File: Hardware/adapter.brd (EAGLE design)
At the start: 61.9 x 62.5 mm, 8 parts

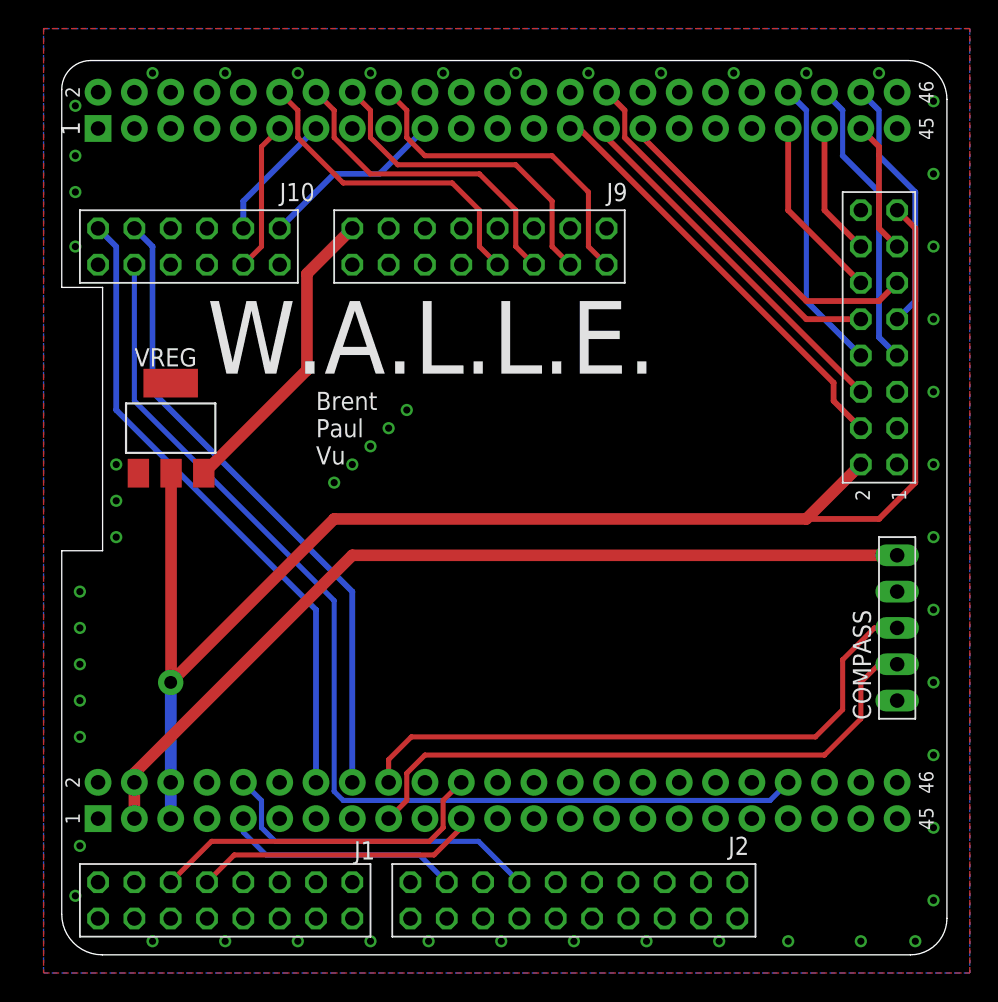
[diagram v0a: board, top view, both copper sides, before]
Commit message: Converted to TI LDO component.
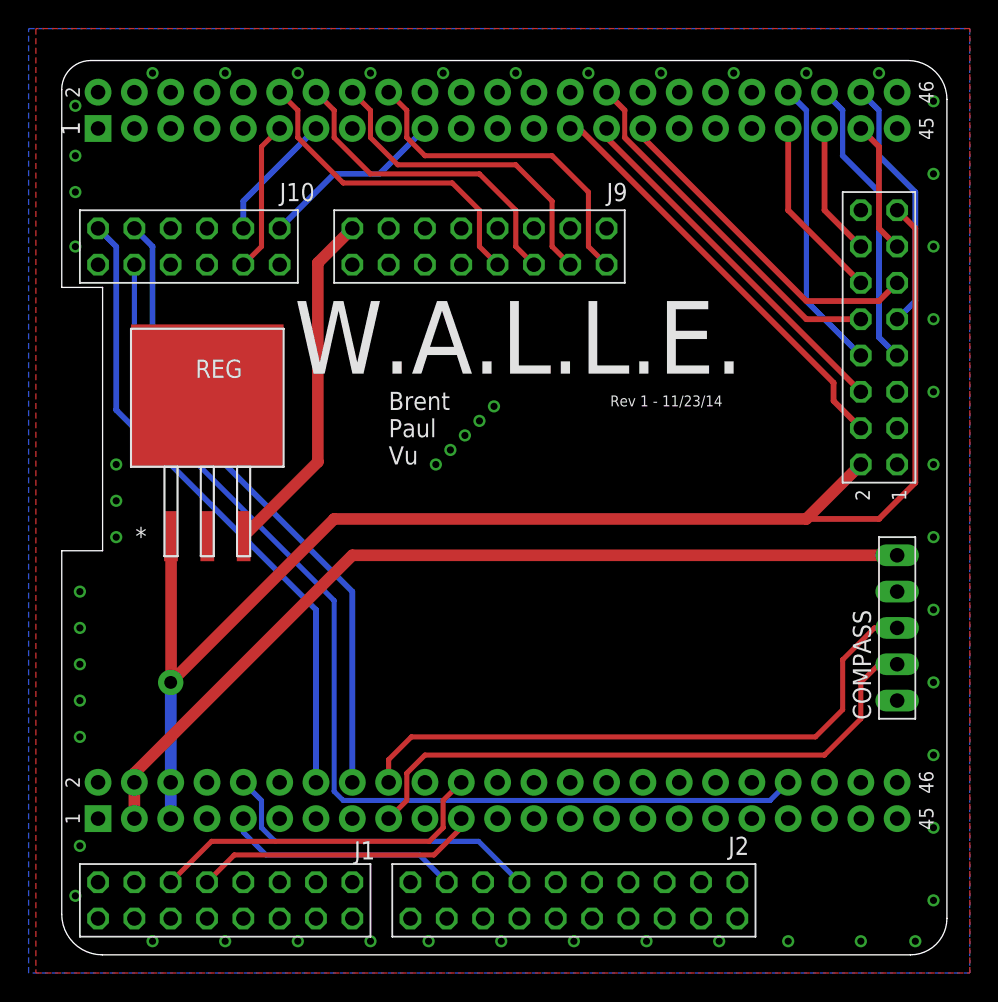
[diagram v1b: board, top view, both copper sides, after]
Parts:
- removed VREG: REG1117, burr-brown:SOT223
- added REG: UCC383-5_KTT_3, TI_UCC:KTT3_6P22X6P6
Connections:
- net 5V: now also REG.1; no longer VREG.2
- net GND: now also REG.2, REG.4; no longer VREG.1
- net VBAT: now also REG.3; no longer VREG.3
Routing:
- net 5V: track 121.6 -> 102.5 mm
- net VBAT: track 21.4 -> 24.7 mm
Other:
- board text added: "Rev 1 - 11/23/14"
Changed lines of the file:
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@@
 <setting verticaltext="up"/>
 </settings>
-<grid distance="0.4" unitdist="mil" unit="mil" style="lines" multiple="1" display="yes" altdistance="10" altunitdist="mil" altunit="mil"/>
+<grid distance="40" unitdist="mil" unit="mil" style="lines" multiple="1" display="yes" altdistance="10" altunitdist="mil" altunit="mil"/>
 <layers>
 <layer number="1" name="Top" color="4" fill="1" visible="yes" active="yes"/>
@@
 <wire x1="26.67" y1="47.9425" x2="29.5275" y2="47.9425" width="0" layer="20"/>
 <wire x1="29.5275" y1="29.5275" x2="26.67" y2="29.5275" width="0" layer="20"/>
-<text x="36.83" y="41.91" size="5.08" layer="21">W.A.L.L.E.</text>
-<text x="44.45" y="35.56" size="1.27" layer="21">Brent
+<text x="42.926" y="41.91" size="5.08" layer="21">W.A.L.L.E.</text>
+<text x="49.53" y="35.56" size="1.27" layer="21">Brent
 Paul
 Vu</text>
@@
 <text x="85.725" y="33.02" size="1.016" layer="25" rot="R90">1</text>
 <text x="83.185" y="33.02" size="1.016" layer="25" rot="R90">2</text>
+<text x="65.024" y="39.624" size="0.762" layer="21">Rev 1 - 11/23/14</text>
 </plain>
 <attributes>
@@
 <attribute name="VALUE" x="66.04" y="46.355" size="1.27" layer="28" rot="MR0"/>
 </element>
-<element name="VREG" library="burr-brown" package="SOT223" value="REG1117" x="34.29" y="38.1">
-<attribute name="OC_NEWARK" value="14P6981" x="34.29" y="38.1" size="1.778" layer="27" display="off"/>
-<attribute name="MPN" value="REG1117" x="34.29" y="38.1" size="1.778" layer="27" display="off"/>
-<attribute name="MF" value="" x="34.29" y="38.1" size="1.778" layer="27" display="off"/>
-<attribute name="OC_FARNELL" value="1097566" x="34.29" y="38.1" size="1.778" layer="27" display="off"/>
-</element>
 <element name="EXTRA" library="pinhead" package="2X08" value="EXT" x="83.82" y="44.45" smashed="yes" rot="R90">
 <attribute name="VALUE" x="80.645" y="41.91" size="1.27" layer="27" rot="R90"/>
+</element>
+<element name="REG" library="TI_UCC" package="KTT3_6P22X6P6" value="UCC383-5_KTT_3" x="36.85031875" y="40.223440625" smashed="yes">
+<attribute name="DATASHEETURL" value="http://www.ti.com/lit/gpn/UCC383-5" x="36.85031875" y="40.223440625" size="1.778" layer="27" display="off"/>
+<attribute name="PIN_COUNT" value="3" x="36.85031875" y="40.223440625" size="1.778" layer="27" display="off"/>
+<attribute name="GENERIC_PART_NUMBER" value="UCC383-5" x="36.85031875" y="40.223440625" size="1.778" layer="27" display="off"/>
+<attribute name="DESCRIPTION" value="Single Output LDO, 3.0A, Fixed(5.0V), Reverse Current Protection, Thermal Shutdown" x="36.85031875" y="40.223440625" size="1.778" layer="27" display="off"/>
+<attribute name="FAMILY_NAME" value="SINGLE CHANNEL LDO" x="36.85031875" y="40.223440625" size="1.778" layer="27" display="off"/>
+<attribute name="MANUFACTURER" value="Texas Instruments" x="36.85031875" y="40.223440625" size="1.778" layer="27" display="off"/>
+<attribute name="INDUSTRY_STD_PKG_TYPE" value="DDPAK/TO-263" x="36.85031875" y="40.223440625" size="1.778" layer="27" display="off"/>
+<attribute name="VENDOR" value="Texas Instruments" x="36.85031875" y="40.223440625" size="1.778" layer="27" display="off"/>
+<attribute name="MANUFACTURER_PART_NUMBER" value="ucc383-5_ktt_3" x="36.85031875" y="40.223440625" size="1.778" layer="27" display="off"/>
+<attribute name="PACKAGE_DESIGNATOR" value="KTT" x="36.85031875" y="40.223440625" size="1.778" layer="27" display="off"/>
+<attribute name="NAME" x="36.01211875" y="41.620440625" size="1.27" layer="25" ratio="6" rot="SR0"/>
 </element>
 </elements>
@@
 <contactref element="U$1" pad="P8.2"/>
 <polygon width="0.4064" layer="1">
-<vertex x="25.4" y="66.04"/>
-<vertex x="25.4" y="0"/>
+<vertex x="24.86151875" y="66.04"/>
+<vertex x="24.86151875" y="0"/>
 <vertex x="90.17" y="0"/>
 <vertex x="90.17" y="66.04"/>
 </polygon>
 <polygon width="0.4064" layer="16">
-<vertex x="25.4" y="66.04"/>
+<vertex x="24.353521875" y="66.04"/>
 <vertex x="90.17" y="66.04"/>
 <vertex x="90.17" y="0"/>
-<vertex x="25.4" y="0"/>
+<vertex x="24.353521875" y="0"/>
 </polygon>
 <via x="87.63" y="30.48" extent="1-16" drill="0.5"/>
@@
 <via x="27.6225" y="54.61" extent="1-16" drill="0.5"/>
 <via x="27.6225" y="57.15" extent="1-16" drill="0.5"/>
-<via x="50.8" y="39.37" extent="1-16" drill="0.5"/>
-<via x="45.72" y="34.29" extent="1-16" drill="0.5"/>
-<via x="46.99" y="35.56" extent="1-16" drill="0.5"/>
-<via x="48.26" y="36.83" extent="1-16" drill="0.5"/>
-<via x="49.53" y="38.1" extent="1-16" drill="0.5"/>
-<contactref element="VREG" pad="1"/>
+<via x="56.896" y="39.624" extent="1-16" drill="0.5"/>
+<via x="52.832" y="35.56" extent="1-16" drill="0.5"/>
+<via x="53.848" y="36.576" extent="1-16" drill="0.5"/>
+<via x="54.864" y="37.592" extent="1-16" drill="0.5"/>
+<via x="55.88" y="38.608" extent="1-16" drill="0.5"/>
 <contactref element="J9" pad="14"/>
 <contactref element="J9" pad="12"/>
@@
 <via x="86.36" y="2.2225" extent="1-16" drill="0.5"/>
 <via x="27.6225" y="60.6425" extent="1-16" drill="0.5"/>
+<contactref element="REG" pad="2"/>
+<contactref element="REG" pad="4"/>
 </signal>
 <signal name="I2C1_SCL">
@@
 </signal>
 <signal name="VBAT">
-<contactref element="VREG" pad="3"/>
 <contactref element="J9" pad="16"/>
-<wire x1="36.6014" y1="34.9504" x2="43.815" y2="42.164" width="0.8128" layer="1"/>
-<wire x1="43.815" y1="42.164" x2="43.815" y2="48.895" width="0.8128" layer="1"/>
-<wire x1="43.815" y1="48.895" x2="46.99" y2="52.07" width="0.8128" layer="1"/>
+<contactref element="REG" pad="3"/>
+<wire x1="39.39031875" y1="30.546040625" x2="44.58208125" y2="35.737803125" width="0.8128" layer="1"/>
+<wire x1="44.58208125" y1="35.737803125" x2="44.58208125" y2="49.66208125" width="0.8128" layer="1"/>
+<wire x1="44.58208125" y1="49.66208125" x2="46.99" y2="52.07" width="0.8128" layer="1"/>
 </signal>
 <signal name="5V">
-<contactref element="VREG" pad="2"/>
 <contactref element="U$1" pad="P9.6"/>
 <contactref element="U$1" pad="P9.5"/>
 <wire x1="34.29" y1="10.795" x2="34.29" y2="13.335" width="0.8128" layer="16"/>
 <wire x1="34.29" y1="13.335" x2="34.29" y2="20.32" width="0.8128" layer="16"/>
-<wire x1="34.3154" y1="34.9504" x2="34.3154" y2="20.3454" width="0.8128" layer="1"/>
-<wire x1="34.3154" y1="20.3454" x2="34.29" y2="20.32" width="0.8128" layer="1"/>
 <via x="34.29" y="20.32" extent="1-16" drill="0.9" diameter="1.778"/>
-<wire x1="34.3154" y1="34.9504" x2="34.29" y2="34.9504" width="0.4064" layer="1"/>
-<wire x1="34.29" y1="34.9504" x2="34.29" y2="20.32" width="0.4064" layer="1"/>
-<wire x1="34.29" y1="20.32" x2="45.72" y2="31.75" width="0.8128" layer="1"/>
+<wire x1="34.29" y1="20.32" x2="34.3154" y2="20.3454" width="0.8128" layer="1"/>
 <contactref element="EXTRA" pad="2"/>
 <contactref element="EXTRA" pad="15"/>
+<wire x1="34.3154" y1="20.3454" x2="45.72" y2="31.75" width="0.8128" layer="1"/>
 <wire x1="45.72" y1="31.75" x2="78.74" y2="31.75" width="0.8128" layer="1"/>
 <wire x1="78.74" y1="31.75" x2="82.55" y2="35.56" width="0.8128" layer="1"/>
@@
 <wire x1="86.36" y1="34.29" x2="83.82" y2="31.75" width="0.4064" layer="1"/>
 <wire x1="83.82" y1="31.75" x2="78.74" y2="31.75" width="0.4064" layer="1"/>
+<contactref element="REG" pad="1"/>
+<wire x1="34.3154" y1="20.3454" x2="34.3154" y2="30.540959375" width="0.8128" layer="1"/>
+<wire x1="34.3154" y1="30.540959375" x2="34.31031875" y2="30.546040625" width="0.8128" layer="1"/>
 </signal>
 <signal name="EX6">

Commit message: Renamed WALLE to AVX on PCB.
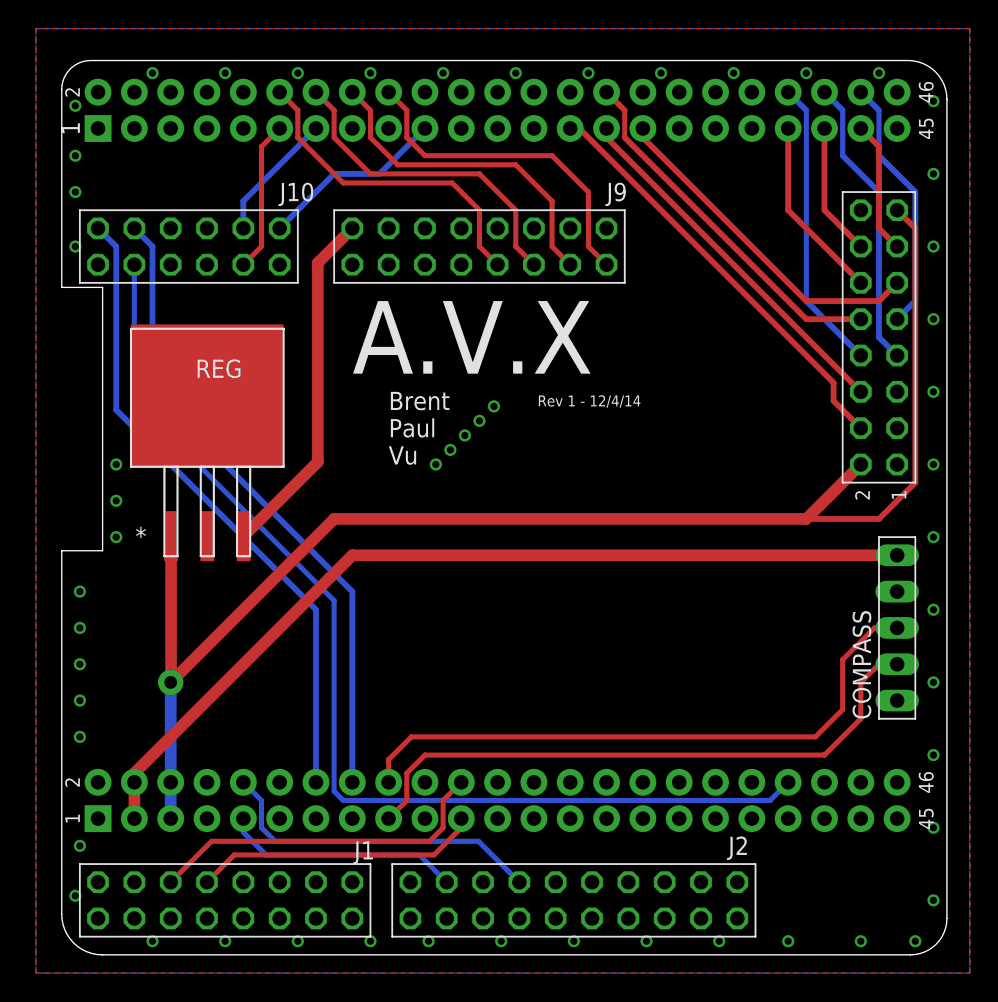
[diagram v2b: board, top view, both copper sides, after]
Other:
- board text added: "A.V.X"
- board text added: "Rev 1 - 12/4/14"
- board text removed: "Rev 1 - 11/23/14"
- board text removed: "W.A.L.L.E."
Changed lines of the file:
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@@
 <wire x1="26.67" y1="47.9425" x2="29.5275" y2="47.9425" width="0" layer="20"/>
 <wire x1="29.5275" y1="29.5275" x2="26.67" y2="29.5275" width="0" layer="20"/>
-<text x="42.926" y="41.91" size="5.08" layer="21">W.A.L.L.E.</text>
+<text x="46.99" y="41.91" size="5.08" layer="21">A.V.X</text>
 <text x="49.53" y="35.56" size="1.27" layer="21">Brent
 Paul
@@
 <text x="85.725" y="33.02" size="1.016" layer="25" rot="R90">1</text>
 <text x="83.185" y="33.02" size="1.016" layer="25" rot="R90">2</text>
-<text x="65.024" y="39.624" size="0.762" layer="21">Rev 1 - 11/23/14</text>
+<text x="59.944" y="39.624" size="0.762" layer="21">Rev 1 - 12/4/14</text>
 </plain>
 <attributes>
@@
 </polygon>
 <polygon width="0.4064" layer="16">
-<vertex x="24.353521875" y="66.04"/>
+<vertex x="24.861521875" y="66.04"/>
 <vertex x="90.17" y="66.04"/>
 <vertex x="90.17" y="0"/>
-<vertex x="24.353521875" y="0"/>
+<vertex x="24.861521875" y="0"/>
 </polygon>
 <via x="87.63" y="30.48" extent="1-16" drill="0.5"/>

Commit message: Fixed issue with pinout for magnetometer. Updated layout ground plane vias.
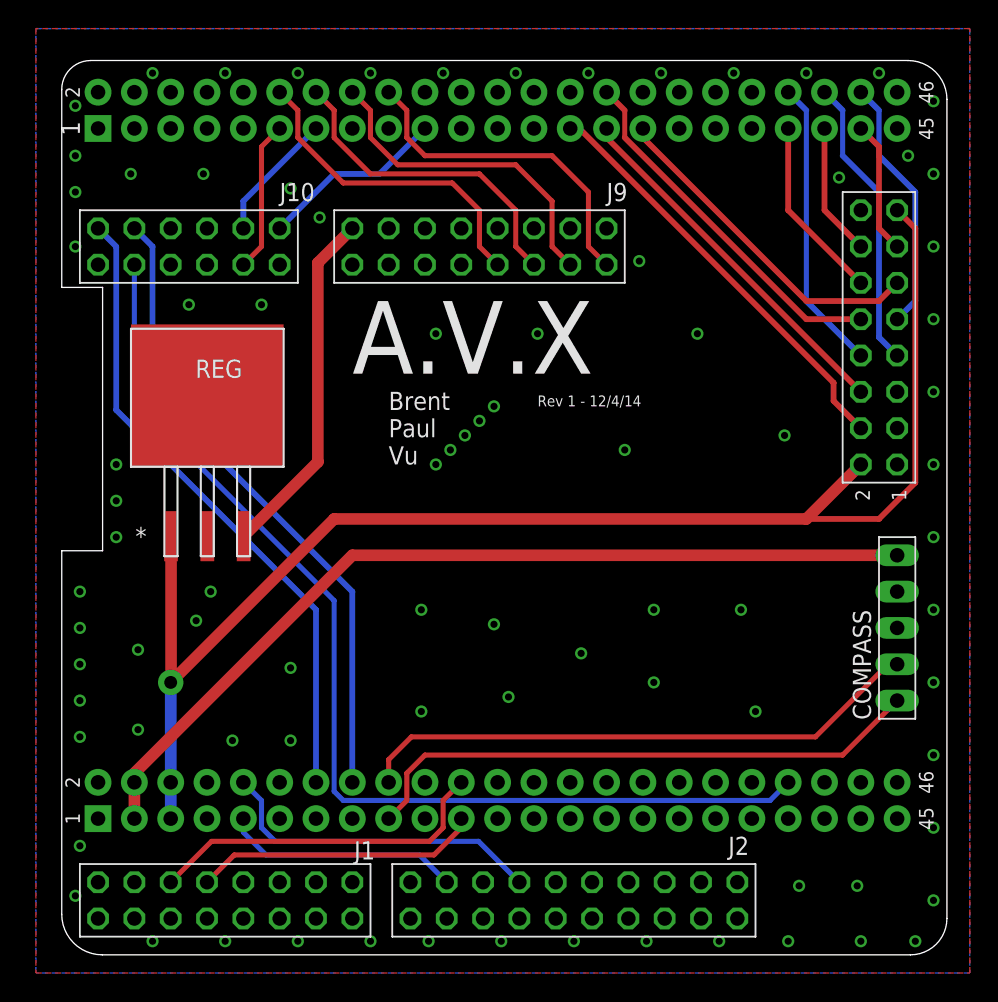
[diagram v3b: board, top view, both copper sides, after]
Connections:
- net I2C1_SCL: now also COMPASS.1; no longer COMPASS.2
- net I2C1_SDA: now also COMPASS.2; no longer COMPASS.3
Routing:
- net I2C1_SDA: track 43.0 -> 39.9 mm
- net I2C1_SCL: track 42.6 -> 40.1 mm
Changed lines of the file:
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@@
 <contactref element="REG" pad="2"/>
 <contactref element="REG" pad="4"/>
+<via x="51.816" y="25.4" extent="1-16" drill="0.5"/>
+<via x="74.168" y="25.4" extent="1-16" drill="0.5"/>
+<via x="75.184" y="18.288" extent="1-16" drill="0.5"/>
+<via x="51.816" y="18.288" extent="1-16" drill="0.5"/>
+<via x="62.992" y="22.352" extent="1-16" drill="0.5"/>
+<via x="38.608" y="16.256" extent="1-16" drill="0.5"/>
+<via x="42.672" y="21.336" extent="1-16" drill="0.5"/>
+<via x="42.672" y="16.256" extent="1-16" drill="0.5"/>
+<via x="37.084" y="26.67" extent="1-16" drill="0.5"/>
+<via x="36.068" y="24.638" extent="1-16" drill="0.5"/>
+<via x="77.216" y="37.592" extent="1-16" drill="0.5"/>
+<via x="71.12" y="44.704" extent="1-16" drill="0.5"/>
+<via x="66.04" y="36.576" extent="1-16" drill="0.5"/>
+<via x="81.026" y="55.626" extent="1-16" drill="0.5"/>
+<via x="85.852" y="57.15" extent="1-16" drill="0.5"/>
+<via x="78.232" y="6.096" extent="1-16" drill="0.5"/>
+<via x="82.296" y="6.096" extent="1-16" drill="0.5"/>
+<via x="68.072" y="20.32" extent="1-16" drill="0.5"/>
+<via x="68.072" y="25.4" extent="1-16" drill="0.5"/>
+<via x="57.912" y="19.304" extent="1-16" drill="0.5"/>
+<via x="56.896" y="24.384" extent="1-16" drill="0.5"/>
+<via x="31.496" y="55.88" extent="1-16" drill="0.5"/>
+<via x="36.576" y="55.88" extent="1-16" drill="0.5"/>
+<via x="32.004" y="22.606" extent="1-16" drill="0.5"/>
+<via x="32.004" y="17.018" extent="1-16" drill="0.5"/>
+<via x="44.704" y="52.832" extent="1-16" drill="0.5"/>
+<via x="40.64" y="46.736" extent="1-16" drill="0.5"/>
+<via x="35.56" y="46.736" extent="1-16" drill="0.5"/>
+<via x="42.672" y="54.864" extent="1-16" drill="0.5"/>
+<via x="67.056" y="49.784" extent="1-16" drill="0.5"/>
+<via x="59.944" y="44.704" extent="1-16" drill="0.5"/>
+<via x="52.832" y="44.704" extent="1-16" drill="0.5"/>
 </signal>
 <signal name="I2C1_SCL">
-<contactref element="COMPASS" pad="2"/>
 <contactref element="U$1" pad="P9.17"/>
 <wire x1="49.53" y1="10.795" x2="50.8" y2="12.065" width="0.3556" layer="1"/>
 <wire x1="50.8" y1="12.065" x2="50.8" y2="13.97" width="0.3556" layer="1"/>
 <wire x1="50.8" y1="13.97" x2="52.07" y2="15.24" width="0.3556" layer="1"/>
-<wire x1="52.07" y1="15.24" x2="80.01" y2="15.24" width="0.3556" layer="1"/>
-<wire x1="80.01" y1="15.24" x2="82.55" y2="17.78" width="0.3556" layer="1"/>
-<wire x1="82.55" y1="17.78" x2="82.55" y2="20.32" width="0.3556" layer="1"/>
-<wire x1="82.55" y1="20.32" x2="83.82" y2="21.59" width="0.3556" layer="1"/>
-<wire x1="83.82" y1="21.59" x2="85.09" y2="21.59" width="0.3556" layer="1"/>
+<wire x1="52.07" y1="15.24" x2="81.28" y2="15.24" width="0.3556" layer="1"/>
+<contactref element="COMPASS" pad="1"/>
+<wire x1="81.28" y1="15.24" x2="85.09" y2="19.05" width="0.3556" layer="1"/>
 </signal>
 <signal name="3.3V">
@@
 </signal>
 <signal name="I2C1_SDA">
-<contactref element="COMPASS" pad="3"/>
 <contactref element="U$1" pad="P9.18"/>
 <wire x1="51.1175" y1="16.51" x2="79.375" y2="16.51" width="0.3556" layer="1"/>
-<wire x1="79.375" y1="16.51" x2="81.28" y2="18.415" width="0.3556" layer="1"/>
-<wire x1="81.28" y1="18.415" x2="81.28" y2="21.9075" width="0.3556" layer="1"/>
-<wire x1="81.28" y1="21.9075" x2="83.5025" y2="24.13" width="0.3556" layer="1"/>
-<wire x1="83.5025" y1="24.13" x2="85.09" y2="24.13" width="0.3556" layer="1"/>
 <wire x1="51.1175" y1="16.51" x2="49.53" y2="14.9225" width="0.3556" layer="1"/>
 <wire x1="49.53" y1="14.9225" x2="49.53" y2="13.335" width="0.3556" layer="1"/>
+<contactref element="COMPASS" pad="2"/>
+<wire x1="79.375" y1="16.51" x2="84.455" y2="21.59" width="0.3556" layer="1"/>
+<wire x1="84.455" y1="21.59" x2="85.09" y2="21.59" width="0.3556" layer="1"/>
 </signal>
 <signal name="LED1">
